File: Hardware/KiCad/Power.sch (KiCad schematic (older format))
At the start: 20 parts, among them J1 USB_MICROB, Q1 2N7002PW, U1 FT231XS

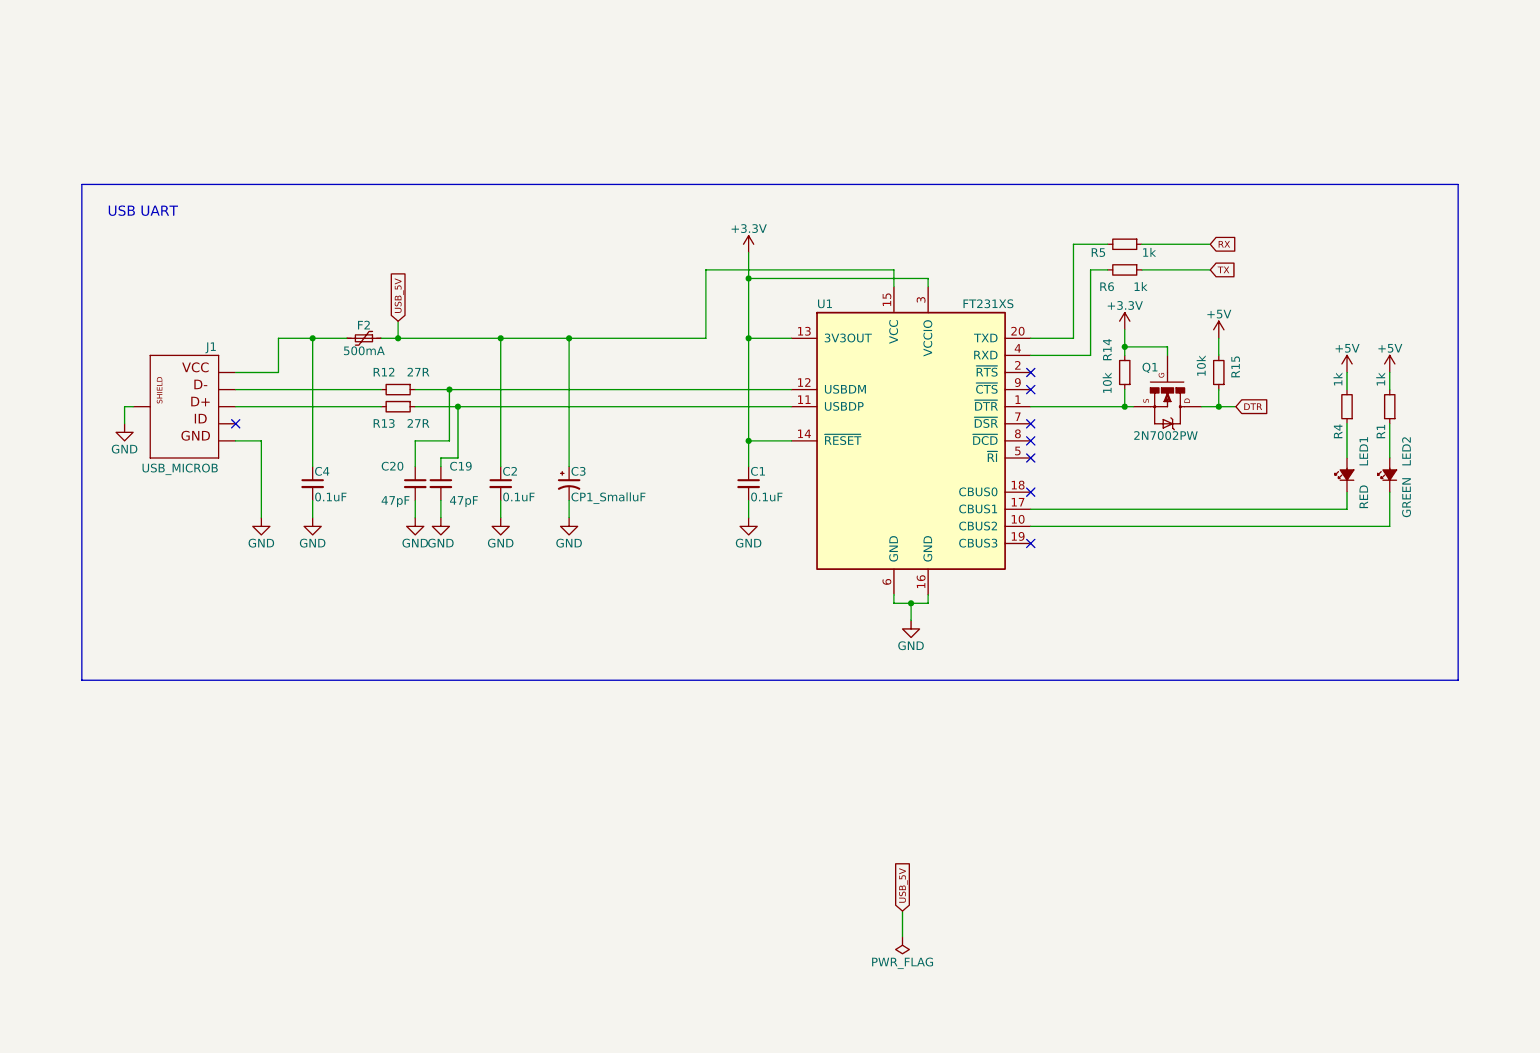
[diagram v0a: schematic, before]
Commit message: Cambiando el árbol de carpetas
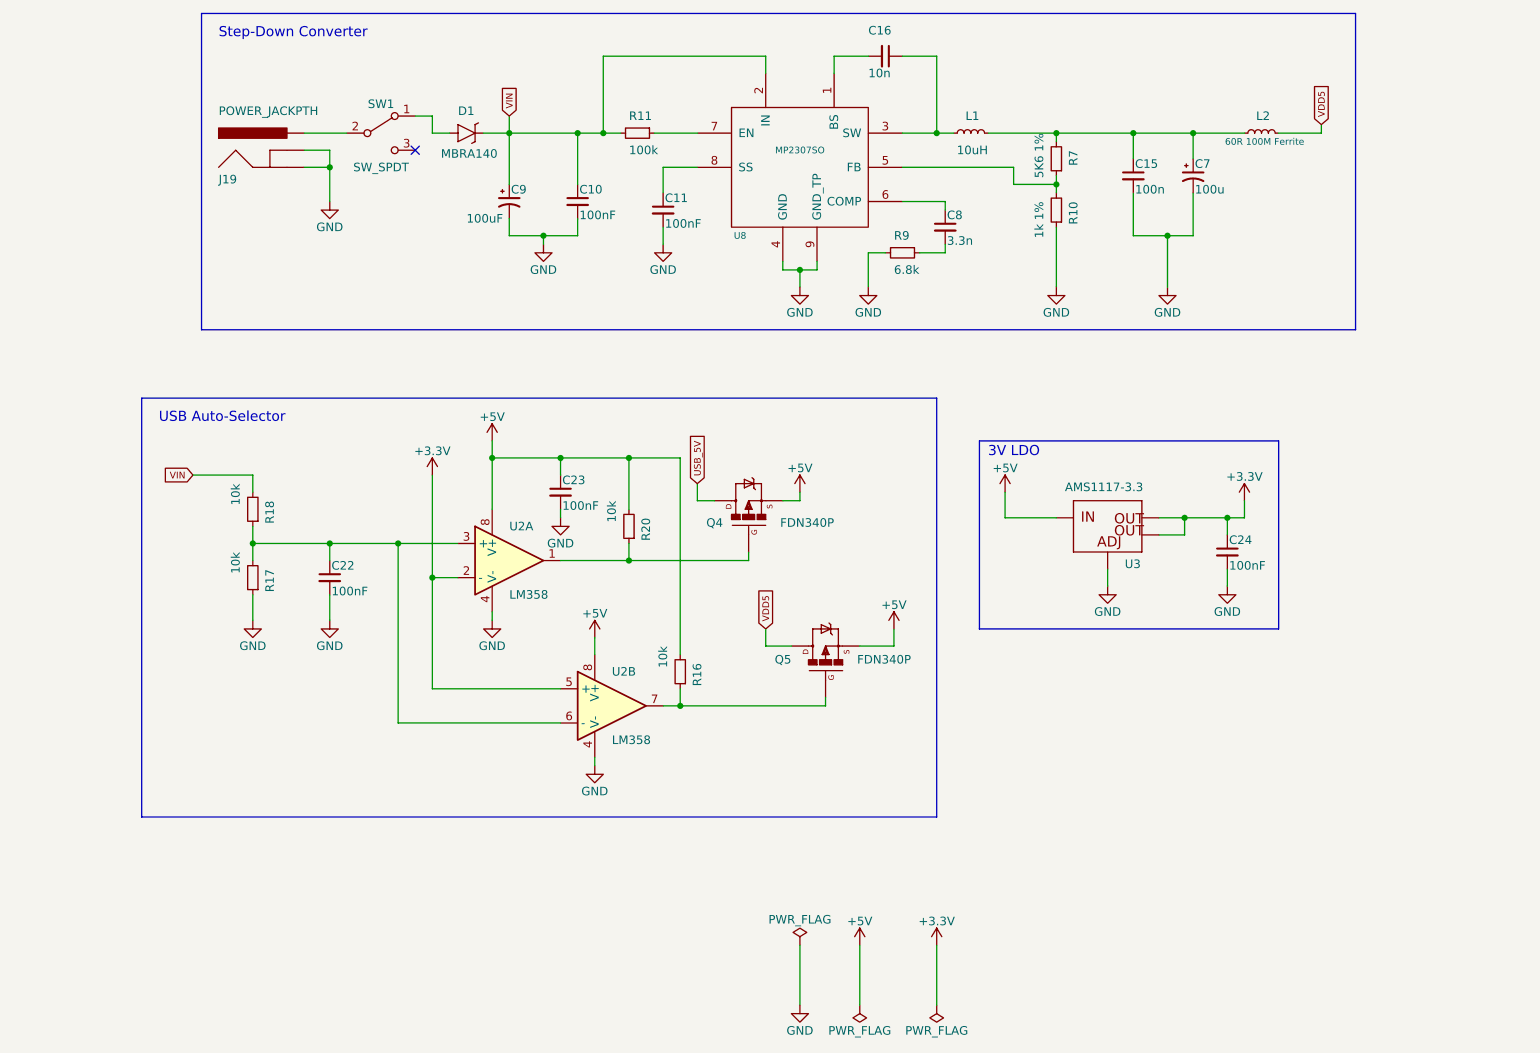
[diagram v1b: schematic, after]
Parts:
- removed C1, C2, C4: 0.1uF, Capacitors_SMD:C_0805, symbol C_Small
- removed C19, C20: 47pF, Capacitors_SMD:C_0805, symbol C_Small
- removed C3: CP1_SmalluF, Capacitors_Tantalum_SMD:CP_Tantalum_Case-A_EIA-3216-18_Reflow, symbol CP1_Small
- removed F2: 500mA, Resistors_SMD:R_1812, symbol Polyfuse_Small
- removed J1: USB_MICROB, Connectors_USB:USB_Micro-B_Molex-105017-0001, symbol USB_MICROB_PLUGCONN-11752
- removed LED1: RED, LEDs:LED_0805, symbol LED_Small_ALT
- removed LED2: GREEN, LEDs:LED_0805, symbol LED_Small_ALT
- removed Q1: 2N7002PW, TO_SOT_Packages_SMD:SOT-323_SC-70, symbol MOSFET-NCHANNEL2N7002PW
- removed R1, R4, R5, R6: 1k, Resistors_SMD:R_0805, symbol R_Small
- removed R12, R13: 27R, Resistors_SMD:R_0805, symbol R_Small
- removed R14, R15: 10k, Resistors_SMD:R_0805, symbol R_Small
- removed U1: FT231XS, SMD_Packages:SSOP-20, symbol FT231XS
- added C10, C11, C22, C23, C24: 100nF, lib_sch:C_0805, symbol C_Small
- added C15: 100n, lib_sch:C_0805, symbol C_Small
- added C16: 10n, lib_sch:C_0805, symbol C_Small
- added C7: 100u, lib_sch:CP_Elec_6.3x5.3, symbol CP1_Small
- added C8: 3.3n, lib_sch:C_0805, symbol C_Small
- added C9: 100uF, lib_sch:CP_Elec_6.3x5.3, symbol CP1_Small
- added D1: MBRA140, lib_sch:D_SMA, symbol MBRA140
- added J19: POWER_JACKPTH, lib_sch:JACK_ALIM, symbol POWER_JACKPTH
- added L1: 10uH, lib_sch:L_Wuerth_WE-PD2-Typ-L, symbol L_Small
- added L2: 60R 100M Ferrite, lib_sch:L_0805, symbol L_Small
- added Q4, Q5: FDN340P, lib_sch:SOT-23, symbol MOSFET-PCHANNEL
- added R10: 1k 1%, lib_sch:R_0805, symbol R_Small
- added R11: 100k, lib_sch:R_0805, symbol R_Small
- added R16, R17, R18, R20: 10k, lib_sch:R_0805, symbol R_Small
- added R7: 5K6 1%, lib_sch:R_0805, symbol R_Small
- added R9: 6.8k, lib_sch:R_0805, symbol R_Small
- added SW1: SW_SPDT, lib_sch:SW_SPDT_PCM12, symbol SW_SPDT
- added U2: LM358, lib_sch:SOIC-8_3.9x4.9mm_Pitch1.27mm, symbol LM358
- added U3: AMS1117-3.3, lib_sch:SOT-223, symbol V_REG_LM1117SOT223
- added U8: MP2307SO, lib_sch:HTSOP-8-1EP_3.9x4.9mm_Pitch1.27mm_ThermalVias_LargeCopper, symbol MP2307SO
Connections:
- net +3V3: now also C24.1, U2.2 (-), U2.5 (+), U3.2 (OUT), U3.4 (OUT)
- net +5V: now also C23.1, Q4.2 (S), Q5.2 (S), R16.2, R20.2, U2.8 (V+), U2.8 (V+), U3.3 (IN)
- net GND: now also C10.2, C11.2, C15.2, C22.2, C23.2, C24.2, C7.2, C9.2, J19.2 (GNDBREAK), J19.3 (GND), R10.1, R17.1, R9.2, U2.4 (V-), U2.4 (V-), U3.1 (ADJ), U8.4 (GND), U8.9 (GND_TP)
- net USB_5V: now also Q4.3 (D)
- new net: C16.2, U8.1 (BS)
- new net: C16.1, L1.1, U8.3 (SW)
- new net: R10.2, R7.1, U8.5 (FB)
- new net: C8.1, U8.6 (COMP)
- new net: R11.1, U8.7 (EN)
- new net: C11.1, U8.8 (SS)
- new net: C8.2, R9.1
- new net: C15.1, C7.1, L1.2, L2.1, R7.2
- new net: Q4.1 (G), R20.1, U2.1
- new net: C22.1, R17.2, R18.1, U2.3 (+), U2.6 (-)
- new net: Q5.1 (G), R16.1, U2.7
- new net: J19.1 (PWR), SW1.2 (B)
- new net: D1.2 (A), SW1.1 (A)
- new net VDD5: L2.2, Q5.3 (D)
- new net VIN: C10.1, C9.1, D1.1 (C), R11.2, R18.2, U8.2 (IN)
- no-connect marks 8 -> 1
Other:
- note added: "3V LDO"
- note added: "Step-Down Converter"
- note added: "USB Auto-Selector"
- note removed: "USB UART\n"

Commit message: Valores cambiados
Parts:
- C15: value 100n -> 100nF
- C16: value 10n -> 10nF
- C7: value 100u -> 100uF
- C8: value 3.3n -> 3.3nF

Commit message: preparando archivos
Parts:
- C10, C11, C15, C16, C22, C23, C24, C8: symbol C_Small -> Grape:C_Small
- C7, C9: symbol CP1_Small -> Grape:CP1_Small
- D1: symbol MBRA140 -> Grape:MBRA140
- J19: symbol POWER_JACKPTH -> Grape:POWER_JACKPTH
- L1, L2: symbol L_Small -> Grape:L_Small
- Q4, Q5: symbol MOSFET-PCHANNEL -> Grape:MOSFET-PCHANNEL
- R10, R11, R16, R17, R18, R20, R7, R9: symbol R_Small -> Grape:R_Small
- SW1: symbol SW_SPDT -> Grape:SW_SPDT
- U2: symbol LM358 -> Grape:LM358
- U3: symbol V_REG_LM1117SOT223 -> Grape:V_REG_LM1117SOT223
- U8: symbol MP2307SO -> Grape:MP2307SO
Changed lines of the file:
@@
-EESchema Schematic File Version 2
-LIBS:Grape
-EELAYER 25 0
+EESchema Schematic File Version 4
+LIBS:Grape-cache
+EELAYER 26 0
 EELAYER END
 $Descr A4 11693 8268
@@
 $EndDescr
 $Comp
-L POWER_JACKPTH J19
+L Grape:POWER_JACKPTH J19
 U 1 1 5A5C9961
 P 2900 2550
@@
 $EndComp
 $Comp
-L MBRA140 D1
+L Grape:MBRA140 D1
 U 1 1 5A5C99D2
 P 3950 2250
@@
 $EndComp
 $Comp
-L SW_SPDT SW1
+L Grape:SW_SPDT SW1
 U 1 1 5A5C9A3B
 P 3450 2250
@@
 	3750 2250 3850 2250
 $Comp
-L GND #PWR077
+L Grape:GND #PWR077
 U 1 1 5A5C9A9A
 P 3150 2650
@@
 Connection ~ 3150 2450
 $Comp
-L MP2307SO U8
+L Grape:MP2307SO U8
 U 1 1 5A5BF038
 P 5900 2450
@@
 $EndComp
 $Comp
-L R_Small R9
+L Grape:R_Small R9
 U 1 1 5A5BF0D7
 P 6500 2950
@@
 $EndComp
 $Comp
-L C_Small C8
+L Grape:C_Small C8
 U 1 1 5A5BF0F6
 P 6750 2800
@@
 $EndComp
 $Comp
-L L_Small L1
+L Grape:L_Small L1
 U 1 1 5A5BF1D1
 P 6900 2250
@@
 $EndComp
 $Comp
-L L_Small L2
+L Grape:L_Small L2
 U 1 1 5A5BF248
 P 8600 2250
@@
 $EndComp
 $Comp
-L LM358 U2
+L Grape:LM358 U2
 U 1 1 5A5BF280
 P 4200 4750
@@
 $EndComp
 $Comp
-L LM358 U2
+L Grape:LM358 U2
 U 2 1 5A5BF2D1
 P 4800 5600
@@
 $EndComp
 $Comp
-L MOSFET-PCHANNEL Q5
+L Grape:MOSFET-PCHANNEL Q5
 U 1 1 5A5BF799
 P 6050 5250
@@
 $EndComp
 $Comp
-L V_REG_LM1117SOT223 U3
+L Grape:V_REG_LM1117SOT223 U3
 U 1 1 5A5BF9C1
 P 7700 4500
@@
 Connection ~ 4200 2250
 $Comp
-L CP1_Small C9
+L Grape:CP1_Small C9
 U 1 1 5A5C0005
 P 4200 2650
@@
 $EndComp
 $Comp
-L GND #PWR078
+L Grape:GND #PWR078
 U 1 1 5A5C01F7
 P 4400 2900
@@
 	4400 2850 4400 2900
 $Comp
-L C_Small C10
+L Grape:C_Small C10
 U 1 1 5A5C02FA
 P 4600 2650
@@
 	4600 2250 4600 2550
 $Comp
-L R_Small R11
+L Grape:R_Small R11
 U 1 1 5A5C056A
 P 4950 2250
@@
 VIN
 $Comp
-L C_Small C11
+L Grape:C_Small C11
 U 1 1 5A5C0F27
 P 5100 2700
@@
 $EndComp
 $Comp
-L GND #PWR079
+L Grape:GND #PWR079
 U 1 1 5A5C0F7F
 P 5100 2900
@@
 	5100 2450 5300 2450
 $Comp
-L GND #PWR080
+L Grape:GND #PWR080
 U 1 1 5A5C10E8
 P 5900 3150
@@
 Connection ~ 5900 3050
 $Comp
-L GND #PWR081
+L Grape:GND #PWR081
 U 1 1 5A5C1430
 P 6300 3150
@@
 	6750 2950 6750 2900
 $Comp
-L C_Small C16
+L Grape:C_Small C16
 U 1 1 5A5C1DE2
 P 6400 1800
@@
 Connection ~ 6700 2250
 $Comp
-L R_Small R7
+L Grape:R_Small R7
 U 1 1 5A5C225B
 P 7400 2400
@@
 $EndComp
 $Comp
-L R_Small R10
+L Grape:R_Small R10
 U 1 1 5A5C23A7
 P 7400 2700
@@
 $EndComp
 $Comp
-L GND #PWR082
+L Grape:GND #PWR082
 U 1 1 5A5C23FE
 P 7400 3150
@@
 Connection ~ 7400 2550
 $Comp
-L CP1_Small C7
+L Grape:CP1_Small C7
 U 1 1 5A5C273B
 P 8200 2500
@@
 $EndComp
 $Comp
-L C_Small C15
+L Grape:C_Small C15
 U 1 1 5A5C28C1
 P 7850 2500
@@
 $EndComp
 $Comp
-L GND #PWR083
+L Grape:GND #PWR083
 U 1 1 5A5C2B61
 P 8050 3150
@@
 VDD5
 $Comp
-L C_Small C22
+L Grape:C_Small C22
 U 1 1 5A5C6DC1
 P 3150 4850
@@
 $EndComp
 $Comp
-L R_Small R18
+L Grape:R_Small R18
 U 1 1 5A5C6FAB
 P 2700 4450
@@
 $EndComp
 $Comp
-L R_Small R17
+L Grape:R_Small R17
 U 1 1 5A5C7277
 P 2700 4850
@@
 $EndComp
 $Comp
-L GND #PWR084
+L Grape:GND #PWR084
 U 1 1 5A5C72FB
 P 2700 5100
@@
 Connection ~ 3150 4650
 $Comp
-L GND #PWR085
+L Grape:GND #PWR085
 U 1 1 5A5C7D92
 P 3150 5100
@@
 	3150 4950 3150 5100
 $Comp
-L +3.3V #PWR086
+L Grape:+3.3V #PWR086
 U 1 1 5A5C80BD
 P 3750 4250
@@
 Connection ~ 3550 4650
 $Comp
-L GND #PWR087
+L Grape:GND #PWR087
 U 1 1 5A5C8333
 P 4100 5100
@@
 	4100 5050 4100 5100
 $Comp
-L GND #PWR088
+L Grape:GND #PWR088
 U 1 1 5A5C859C
 P 4700 5950
@@
 $EndComp
 $Comp
-L +5V #PWR089
+L Grape:+5V #PWR089
 U 1 1 5A5C88D0
 P 4700 5200
@@
 	6450 5250 6450 5150
 $Comp
-L MOSFET-PCHANNEL Q4
+L Grape:MOSFET-PCHANNEL Q4
 U 1 1 5A5BF6D6
 P 5600 4400
@@
 	4500 4750 5600 4750
 $Comp
-L R_Small R20
+L Grape:R_Small R20
 U 1 1 5A5C9C0D
 P 4900 4550
@@
 Connection ~ 4900 4750
 $Comp
-L R_Small R16
+L Grape:R_Small R16
 U 1 1 5A5C9ECA
 P 5200 5400
@@
 	4900 4150 4900 4450
 $Comp
-L C_Small C23
+L Grape:C_Small C23
 U 1 1 5A5CA56B
 P 4500 4350
@@
 $EndComp
 $Comp
-L GND #PWR090
+L Grape:GND #PWR090
 U 1 1 5A5CA6CD
 P 4500 4500
@@
 Connection ~ 4900 4150
 $Comp
-L +5V #PWR091
+L Grape:+5V #PWR091
 U 1 1 5A5CA8D5
 P 4100 4050
@@
 	5600 4750 5600 4700
 $Comp
-L +5V #PWR092
+L Grape:+5V #PWR092
 U 1 1 5A5CB171
 P 5900 4350
@@
 	5900 4400 5900 4350
 $Comp
-L +5V #PWR093
+L Grape:+5V #PWR093
 U 1 1 5A5CB2A8
 P 6450 5150
@@
 	4700 5900 4700 5950
 $Comp
-L PWR_FLAG #FLG094
+L Grape:PWR_FLAG #FLG094
 U 1 1 5A5CCC7F
 P 6700 7350
@@
 $EndComp
 $Comp
-L PWR_FLAG #FLG095
+L Grape:PWR_FLAG #FLG095
 U 1 1 5A5CCD01
 P 6250 7350
@@
 $EndComp
 $Comp
-L PWR_FLAG #FLG096
+L Grape:PWR_FLAG #FLG096
 U 1 1 5A5CCF50
 P 5900 7000
@@
 $EndComp
 $Comp
-L GND #PWR097
+L Grape:GND #PWR097
 U 1 1 5A5CCFAF
 P 5900 7350
@@
 	5900 7350 5900 7000
 $Comp
-L +5V #PWR098
+L Grape:+5V #PWR098
 U 1 1 5A5CD193
 P 6250 7000
@@
 	6250 7000 6250 7350
 $Comp
-L +3.3V #PWR099
+L Grape:+3.3V #PWR099
 U 1 1 5A5CD3CC
 P 6700 7000
@@
 $EndComp
 $Comp
-L C_Small C24
+L Grape:C_Small C24
 U 1 1 5A5CD924
 P 8400 4700
@@
 $EndComp
 $Comp
-L +5V #PWR0100
+L Grape:+5V #PWR0100
 U 1 1 5A5CDF65
 P 7100 4350
@@
 	7100 4500 7400 4500
 $Comp
-L GND #PWR0101
+L Grape:GND #PWR0101
 U 1 1 5A5CE207
 P 7700 4900
@@
 	8000 4500 8500 4500
 $Comp
-L GND #PWR0102
+L Grape:GND #PWR0102
 U 1 1 5A5CE552
 P 8400 4900
@@
 Connection ~ 8400 4500
 $Comp
-L +3.3V #PWR0103
+L Grape:+3.3V #PWR0103
 U 1 1 5A5CEA4E
 P 8500 4400
@@
 $Bitmap
 Pos 10850 6250
-Scale 0,950000
+Scale 0.000000
 Data
 89 50 4E 47 0D 0A 1A 0A 00 00 00 0D 49 48 44 52 00 00 00 C1 00 00 00 8F 08 06 00 00 00 43 10 BF
@@
 $Bitmap
 Pos 7300 6700
-Scale 0,950000
+Scale 0.000000
 Data
 89 50 4E 47 0D 0A 1A 0A 00 00 00 0D 49 48 44 52 00 00 00 91 00 00 00 36 08 06 00 00 00 C7 C1 7B

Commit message: Esquema terminado
Falta comprobar
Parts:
- removed C22, C23: 100nF, lib_sch:C_0805, symbol Grape:C_Small
- removed Q4, Q5: FDN340P, lib_sch:SOT-23, symbol Grape:MOSFET-PCHANNEL
- removed R16, R17, R18, R20: 10k, lib_sch:R_0805, symbol Grape:R_Small
- removed U2: LM358, lib_sch:SOIC-8_3.9x4.9mm_Pitch1.27mm, symbol Grape:LM358
- added Q?: FDN340P, lib_sch:SOT-23, symbol Grape:MOSFET-PCHANNEL
- added R?: 10k, lib_sch:R_0805, symbol Grape:R_Small
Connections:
- net VDD5 is gone; now on net +5V: L2.2
- net +5V: now also Q?.2 (S), R?.2
- net GND: no longer J19.3 (GND)
- net USB_5V: now also Q?.3 (D)
- new net: J19.3 (GND), Q?.1 (G), R?.1
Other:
- note removed: "USB Auto-Selector"
- moved on the sheet: C10, C11, C15, C16, C24, C7, C8, C9, D1, J19, L1, L2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
